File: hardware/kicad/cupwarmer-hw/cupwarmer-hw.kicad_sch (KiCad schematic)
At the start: 3 parts

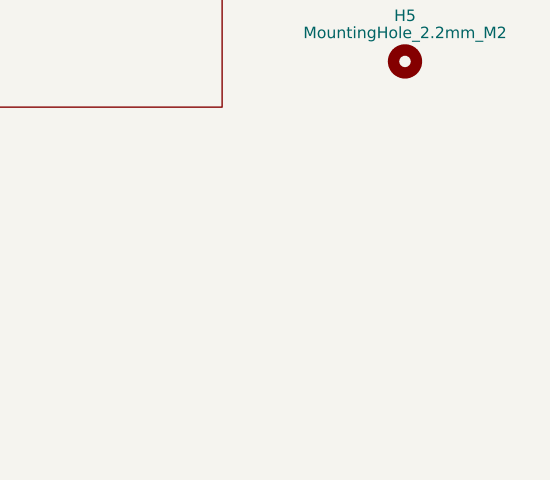
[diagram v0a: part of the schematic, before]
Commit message: Add fiducials, R4 thermal spacing, off-board parts checklist
Continuation of docs/plans/20260517-pre-order-review-issues.md
review pass:

- FID1/FID2/FID3 (Mechanical:Fiducial + Fiducial_1mm_Mask3mm):
  near H3/H4/H5 mounting holes to satisfy WLCSP40 outsourced SMT
  alignment requirement. FID2 offset to (120, 117.5) because the
  HEATER_OUT zone occupied the original (112, 112) target.
  in_bom=false, on_board=true.
- R4 moved (87, 110.4) -> (87, 109.2) for thermal separation from
  R14 (now 3.2mm center-to-center vs prior 2mm) during IEXT SOVP
  pulses.
- design-notes: heater pigtail extraction direction constraint
  (must exit PCB perpendicular to edge, not loop around the board,
  to avoid AC magnetic coupling into FOD); off-board parts
  procurement checklist (F1, heater, TH2, L1, SHIELD1).

Co-Authored-By: Claude Opus 4.7 (1M context) <noreply@anthropic.com>
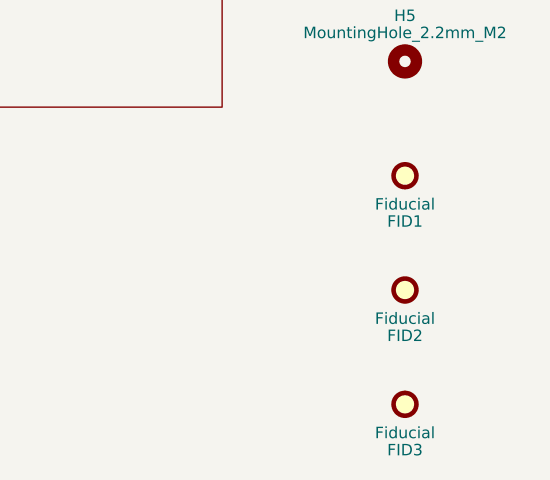
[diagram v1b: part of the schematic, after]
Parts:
- added FID1, FID2, FID3: Fiducial, Fiducial:Fiducial_1mm_Mask3mm, symbol Mechanical:Fiducial
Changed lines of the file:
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@@
 	)
 	(embedded_fonts no)
+	(symbol
+		(lib_id "Mechanical:Fiducial")
+		(at 177.8 86.36 0)
+		(unit 1)
+		(exclude_from_sim no)
+		(in_bom no)
+		(on_board yes)
+		(in_pos_files yes)
+		(dnp no)
+		(property "Reference" "FID1"
+			(at 177.8 91.44 0)
+			(show_name no)
+			(do_not_autoplace no)
+			(effects
+				(font
+					(size 1.27 1.27)
+				)
+			)
+		)
+		(property "Value" "Fiducial"
+			(at 177.8 89.535 0)
+			(show_name no)
+			(do_not_autoplace no)
+			(effects
+				(font
+					(size 1.27 1.27)
+				)
+			)
+		)
+		(property "Footprint" "Fiducial:Fiducial_1mm_Mask3mm"
+			(at 177.8 86.36 0)
+			(show_name no)
+			(do_not_autoplace no)
+			(hide yes)
+			(effects
+				(font
+					(size 1.27 1.27)
+				)
+			)
+		)
+		(property "Datasheet" ""
+			(at 177.8 86.36 0)
+			(show_name no)
+			(do_not_autoplace no)
+			(hide yes)
+			(effects
+				(font
+					(size 1.27 1.27)
+				)
+			)
+		)
+		(property "Description" "Fiducial Marker"
+			(at 177.8 86.36 0)
+			(show_name no)
+			(do_not_autoplace no)
+			(hide yes)
+			(effects
+				(font
+					(size 1.27 1.27)
+				)
+			)
+		)
+		(instances
+			(project "cupwarmer-hw"
+				(path "/f3c63676-f392-4700-9f58-a6787e1eb284"
+					(reference "FID1")
+					(unit 1)
+				)
+			)
+		)
+	)
+	(symbol
+		(lib_id "Mechanical:Fiducial")
+		(at 177.8 111.76 0)
+		(unit 1)
+		(exclude_from_sim no)
+		(in_bom no)
+		(on_board yes)
+		(in_pos_files yes)
+		(dnp no)
+		(property "Reference" "FID3"
+			(at 177.8 116.84 0)
+			(show_name no)
+			(do_not_autoplace no)
+			(effects
+				(font
+					(size 1.27 1.27)
+				)
+			)
+		)
+		(property "Value" "Fiducial"
+			(at 177.8 114.935 0)
+			(show_name no)
+			(do_not_autoplace no)
+			(effects
+				(font
+					(size 1.27 1.27)
+				)
+			)
+		)
+		(property "Footprint" "Fiducial:Fiducial_1mm_Mask3mm"
+			(at 177.8 111.76 0)
+			(show_name no)
+			(do_not_autoplace no)
+			(hide yes)
+			(effects
+				(font
+					(size 1.27 1.27)
+				)
+			)
+		)
+		(property "Datasheet" ""
+			(at 177.8 111.76 0)
+			(show_name no)
+			(do_not_autoplace no)
+			(hide yes)
+			(effects
+				(font
+					(size 1.27 1.27)
+				)
+			)
+		)
+		(property "Description" "Fiducial Marker"
+			(at 177.8 111.76 0)
+			(show_name no)
+			(do_not_autoplace no)
+			(hide yes)
+			(effects
+				(font
+					(size 1.27 1.27)
+				)
+			)
+		)
+		(instances
+			(project "cupwarmer-hw"
+				(path "/f3c63676-f392-4700-9f58-a6787e1eb284"
+					(reference "FID3")
+					(unit 1)
+				)
+			)
+		)
+	)
+	(symbol
+		(lib_id "Mechanical:Fiducial")
+		(at 177.8 99.06 0)
+		(unit 1)
+		(exclude_from_sim no)
+		(in_bom no)
+		(on_board yes)
+		(in_pos_files yes)
+		(dnp no)
+		(property "Reference" "FID2"
+			(at 177.8 104.14 0)
+			(show_name no)
+			(do_not_autoplace no)
+			(effects
+				(font
+					(size 1.27 1.27)
+				)
+			)
+		)
+		(property "Value" "Fiducial"
+			(at 177.8 102.235 0)
+			(show_name no)
+			(do_not_autoplace no)
+			(effects
+				(font
+					(size 1.27 1.27)
+				)
+			)
+		)
+		(property "Footprint" "Fiducial:Fiducial_1mm_Mask3mm"
+			(at 177.8 99.06 0)
+			(show_name no)
+			(do_not_autoplace no)
+			(hide yes)
+			(effects
+				(font
+					(size 1.27 1.27)
+				)
+			)
+		)
+		(property "Datasheet" ""
+			(at 177.8 99.06 0)
+			(show_name no)
+			(do_not_autoplace no)
+			(hide yes)
+			(effects
+				(font
+					(size 1.27 1.27)
+				)
+			)
+		)
+		(property "Description" "Fiducial Marker"
+			(at 177.8 99.06 0)
+			(show_name no)
+			(do_not_autoplace no)
+			(hide yes)
+			(effects
+				(font
+					(size 1.27 1.27)
+				)
+			)
+		)
+		(instances
+			(project "cupwarmer-hw"
+				(path "/f3c63676-f392-4700-9f58-a6787e1eb284"
+					(reference "FID2")
+					(unit 1)
+				)
+			)
+		)
+	)
 )
